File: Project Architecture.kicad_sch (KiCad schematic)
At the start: 0 parts

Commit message: Self-contained libraries, JLCPCB rules, ERC/DRC cleanup
- lib/: project symbol library (19 symbols), footprint library (17 footprints)
  and all 3D models (15), referenced through ${KIPRJMOD} + project lib tables.
  A fresh clone now opens with every symbol, footprint and 3D model.
- Remove duplicated / absolute 3D model paths (C:/Users/..., ${KICAD_FOOTPRINT})
- OPEN_WEIGHT.kicad_dru: JLCPCB 4-layer rules; stackup JLC04161H-7628; board minimums
- AD7190 footprint: drop per-pad 0.102 mm mask margin (mask bridges at 0.65 mm pitch)
- Exclude unplaced TP/FID symbols from board; PWR_FLAGs; decorative wires -> lines
- Local text variables in .kicad_pro; Revision History wired to [Unreleased]
- get_changelog.py: accept "## [Unreleased]" without date
ERC: 0 errors. DRC: 0 errors except 10 courtyard overlaps (placement), 0 parity issues.

Co-Authored-By: Claude Opus 5.5 <noreply@anthropic.com>
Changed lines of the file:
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@@
 		)
 	)
-	(wire
+	(polyline
 		(pts
 			(xy 185.42 161.29) (xy 166.37 161.29)
@@
 		)
 	)
-	(wire
+	(polyline
 		(pts
 			(xy 166.37 132.08) (xy 166.37 161.29)
@@
 		)
 	)
-	(wire
+	(polyline
 		(pts
 			(xy 222.25 161.29) (xy 265.43 161.29)
@@
 		)
 	)
-	(wire
+	(polyline
 		(pts
 			(xy 265.43 132.08) (xy 265.43 161.29)

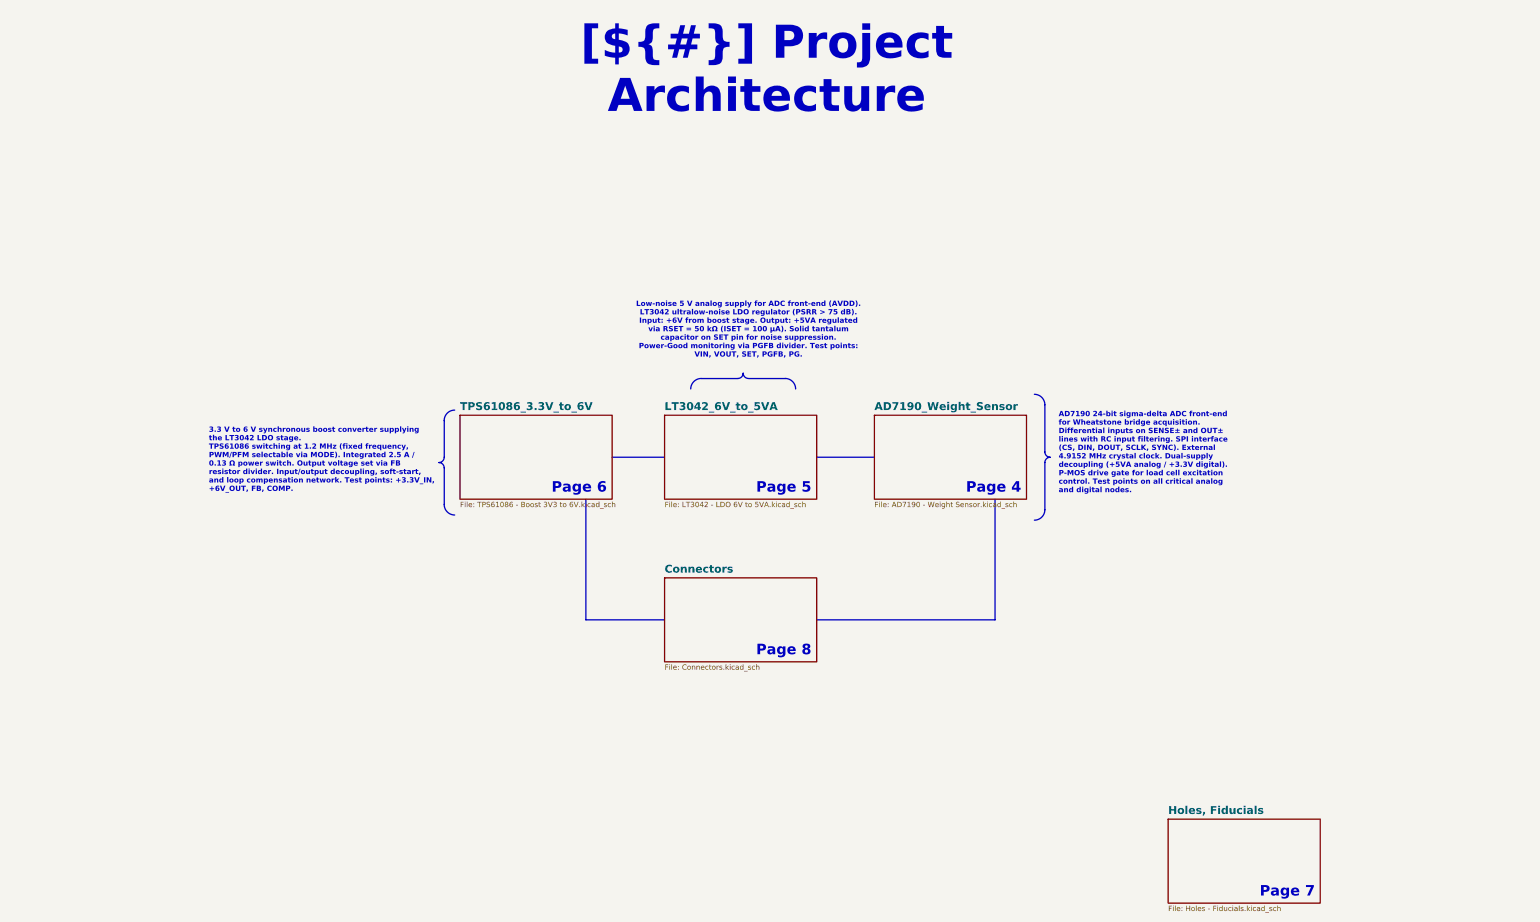
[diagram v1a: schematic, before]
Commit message: Redesign Project Architecture sheet, update dates, refresh netlists
- Project Architecture: aligned hierarchy blocks with per-sheet summaries,
  power chain (+3.3V -> +6V -> +5VA), host <-> AD7190 links, legend and
  hyperlinked document index
- Title-block date set to 2026-09-29 on all sheets
- Regenerate OPEN_WEIGHT.xml / OPEN_WEIGHT-netlist.net with KiCad 10

Co-Authored-By: Claude Opus 5.5 <noreply@anthropic.com>
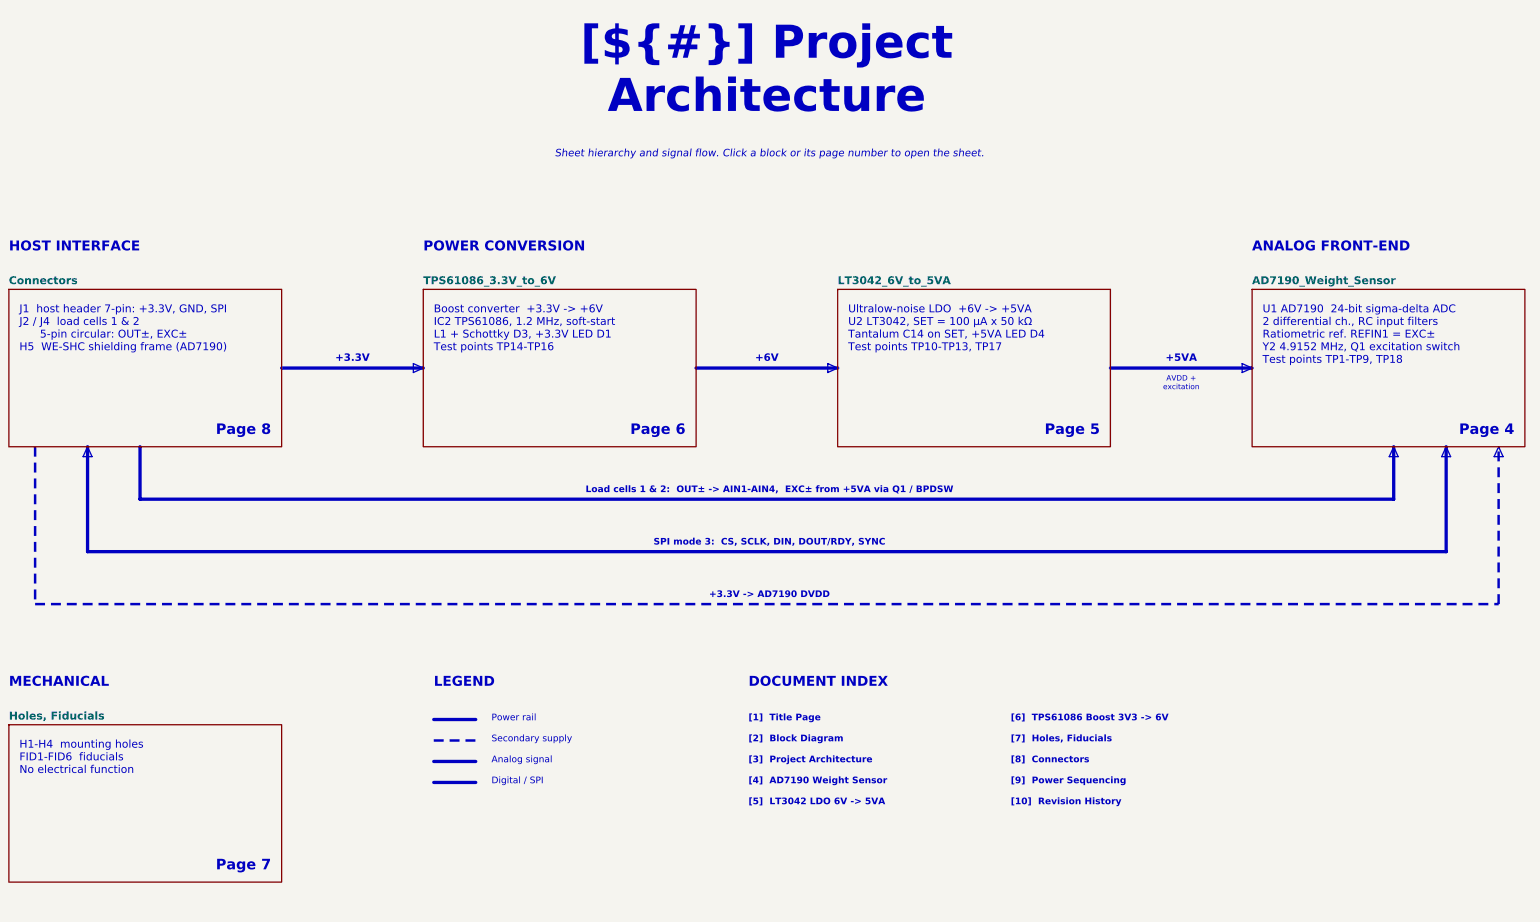
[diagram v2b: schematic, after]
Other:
- note added: "+3.3V"
- note added: "+3.3V -> AD7190 DVDD"
- note added: "+5VA"
- note added: "+6V"
- note added: "ANALOG FRONT-END"
- note added: "AVDD + excitation"
- note added: "Analog signal"
- note added: "Boost converter +3.3V -> +6V IC2 TPS61086, 1.2 MHz, soft-start L1 + Schottky D3, +3.3V LED D1 Test points TP14-TP16"
- note added: "DOCUMENT INDEX"
- note added: "Digital / SPI"
- note added: "H1-H4 mounting holes FID1-FID6 fiducials No electrical function"
- note added: "HOST INTERFACE"
- note added: "J1 host header 7-pin: +3.3V, GND, SPI J2 / J4 load cells 1 & 2 5-pin circular: OUT±, EXC± H5 WE-SHC shielding frame (AD7190)"
- note added: "LEGEND"
- note added: "Load cells 1 & 2: OUT± -> AIN1-AIN4, EXC± from +5VA via Q1 / BPDSW"
- note added: "MECHANICAL"
- note added: "POWER CONVERSION"
- note added: "Power rail"
- note added: "SPI mode 3: CS, SCLK, DIN, DOUT/RDY, SYNC"
- note added: "Secondary supply"
- note added: "Sheet hierarchy and signal flow. Click a block or its page number to open the sheet."
- note added: "U1 AD7190 24-bit sigma-delta ADC 2 differential ch., RC input filters Ratiometric ref. REFIN1 = EXC± Y2 4.9152 MHz, Q1 excitation switch Test points TP1-TP9, TP18"
- note added: "Ultralow-noise LDO +6V -> +5VA U2 LT3042, SET = 100 µA x 50 kΩ Tantalum C14 on SET, +5VA LED D4 Test points TP10-TP13, TP17"
- note added: "[10] Revision History"
- note added: "[1] Title Page"
- note added: "[2] Block Diagram"
- note added: "[3] Project Architecture"
- note added: "[4] AD7190 Weight Sensor"
- note added: "[5] LT3042 LDO 6V -> 5VA"
- note added: "[6] TPS61086 Boost 3V3 -> 6V"
- note added: "[7] Holes, Fiducials"
- note added: "[8] Connectors"
- note added: "[9] Power Sequencing"
